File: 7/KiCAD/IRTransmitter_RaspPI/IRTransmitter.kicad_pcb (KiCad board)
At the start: 2 copper layers, 24.1 x 42.5 mm, 12 parts, among them J1 Conn_02x08_Odd_Even, Q1 BC33740TA, Q2 BC33740TA

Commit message: Optimizing PCB
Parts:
- moved D4 0.41 mm to (64.2, 105.7)
- moved D1 0.20 mm to (76.5, 82.8)
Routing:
- net GND: track 48.3 -> 53.2 mm
- net Net-(D3-Pad1): track 45.3 -> 50.0 mm
- net Net-(D4-Pad2): track 54.0 -> 57.3 mm
- net /GPIO18: track 50.1 -> 48.6 mm
- net +5V: track 52.5 -> 51.4 mm
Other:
- board size 24.1 x 42.5 mm -> 22.9 x 40.6 mm

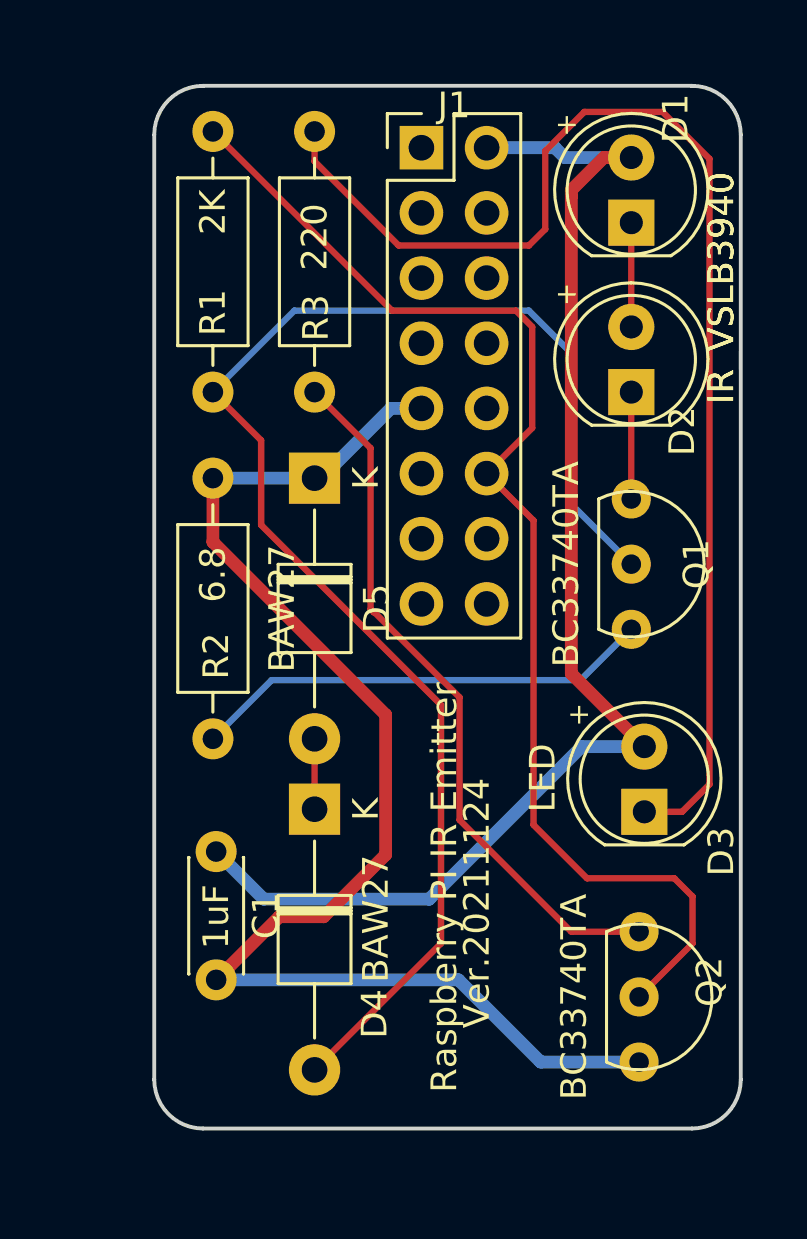
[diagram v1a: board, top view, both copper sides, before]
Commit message: Corrected RaspPI IR emitter.
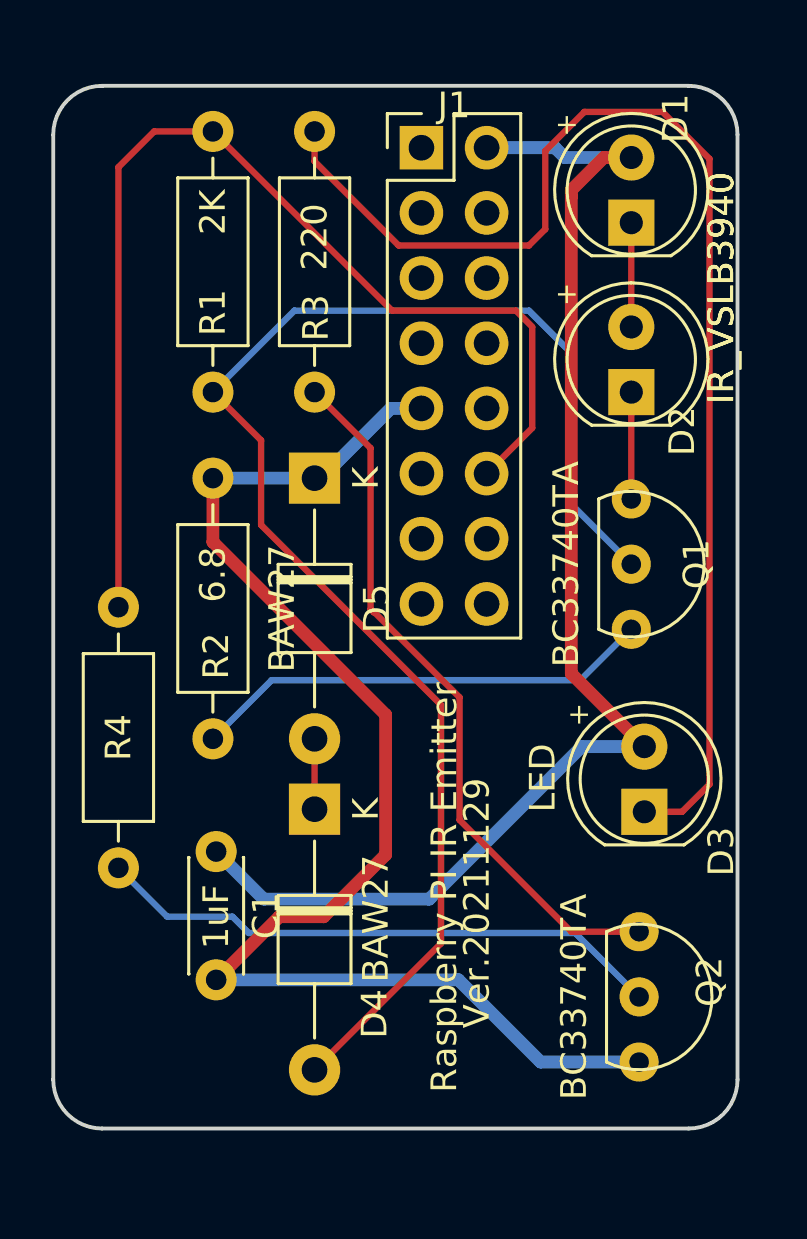
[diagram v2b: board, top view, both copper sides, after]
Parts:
- added R4: 2K, Resistor_THT:R_Axial_DIN0207_L6.3mm_D2.5mm_P10.16mm_Horizontal, F.Cu at (56.5, 108.0)
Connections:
- Q2 pad 2: /GPIO18 -> Net-(Q2-Pad2)
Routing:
- net Net-(Q2-Pad2): track 0.00 -> 22.4 mm
- net /GPIO18: track 48.6 -> 43.5 mm
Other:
- board size 22.9 x 40.6 mm -> 26.7 x 40.6 mm
- board text added: "Ver.20211129"
- board text removed: "Ver.20211124"

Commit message: Corrected RaspPI IR emitter.
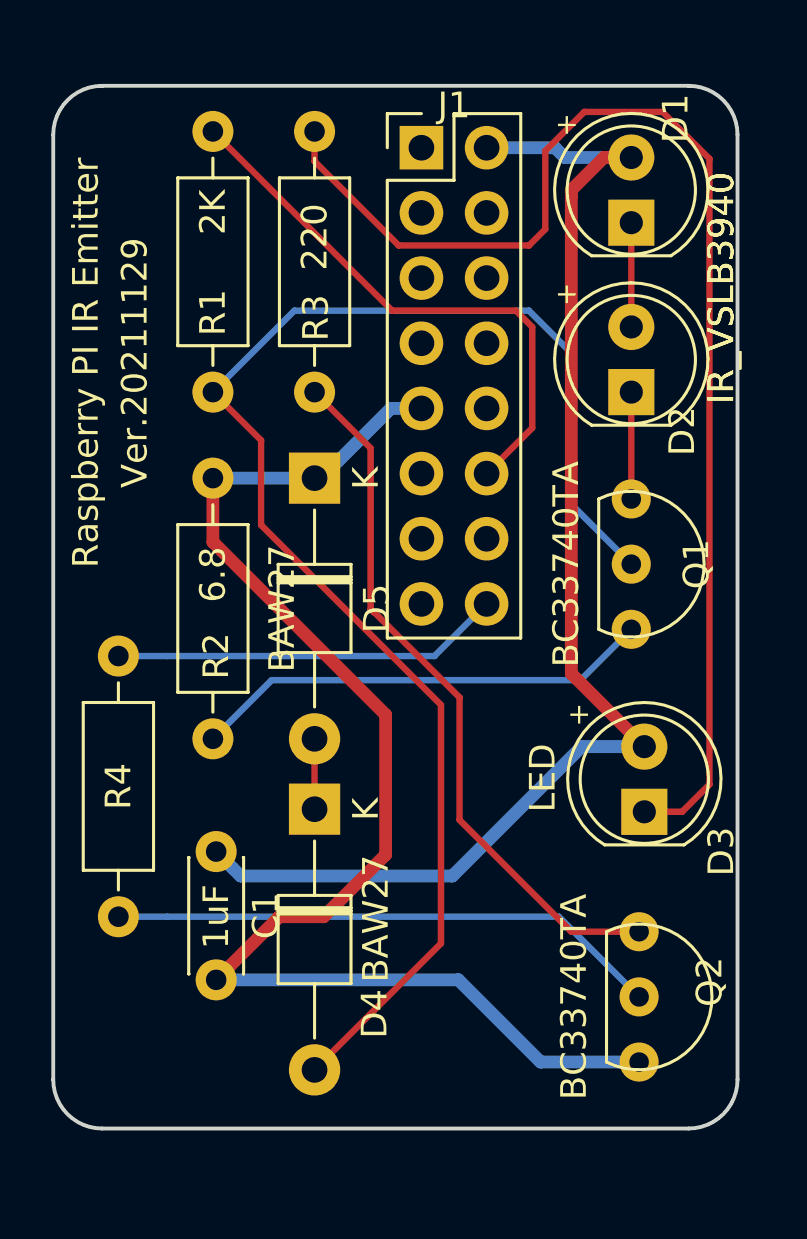
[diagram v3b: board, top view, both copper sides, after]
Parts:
- moved R4 1.91 mm to (56.5, 109.9)
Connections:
- J1 pad 16: Net-(J1-Pad16) -> /GPIO23
- R4 pad 2: /GPIO18 -> /GPIO23
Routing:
- net /GPIO18: track 43.5 -> 22.1 mm
- net /GPIO23: track 0.00 -> 15.2 mm
- net Net-(Q2-Pad2): track 22.4 -> 21.6 mm
- net +5V: track 51.4 -> 50.7 mm

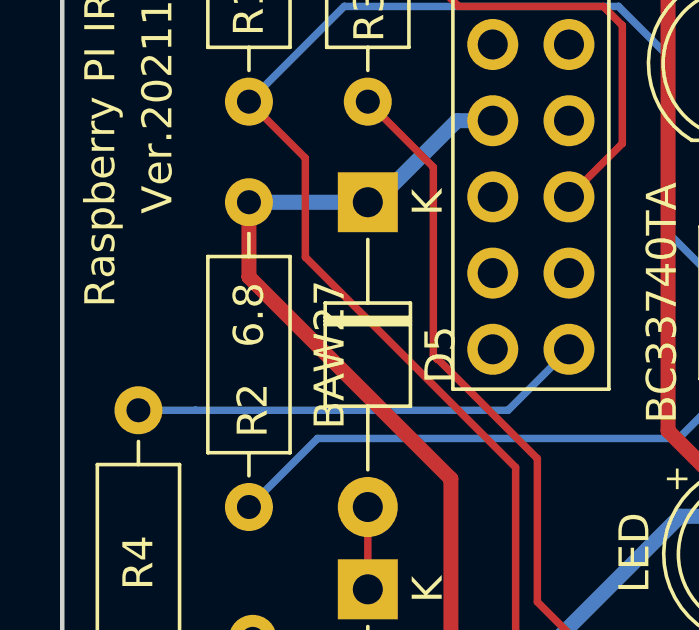
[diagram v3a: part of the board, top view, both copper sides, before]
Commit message: Updated schematic/PCB of RaspPI IR Emitter.
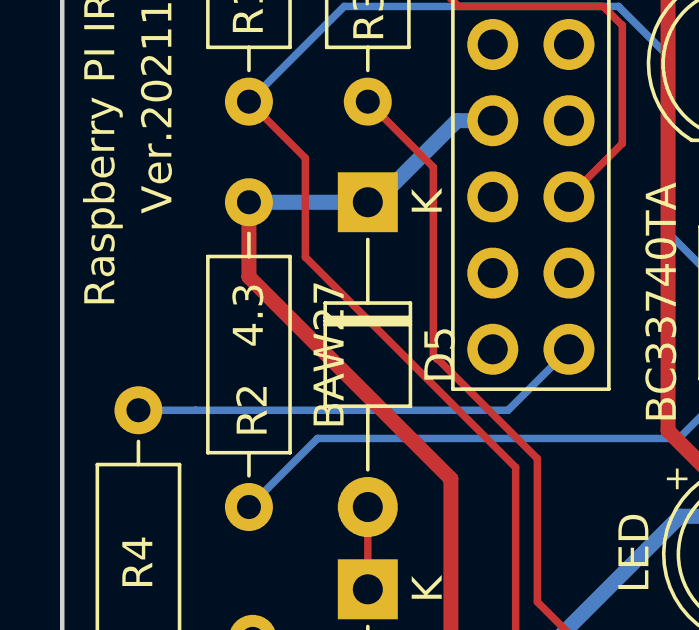
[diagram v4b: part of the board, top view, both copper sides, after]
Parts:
- R2: value 6.8 -> 4.3
